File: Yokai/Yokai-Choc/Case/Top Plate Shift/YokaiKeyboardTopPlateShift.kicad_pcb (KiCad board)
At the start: 2 copper layers, 160.3 x 114.7 mm, 6 parts

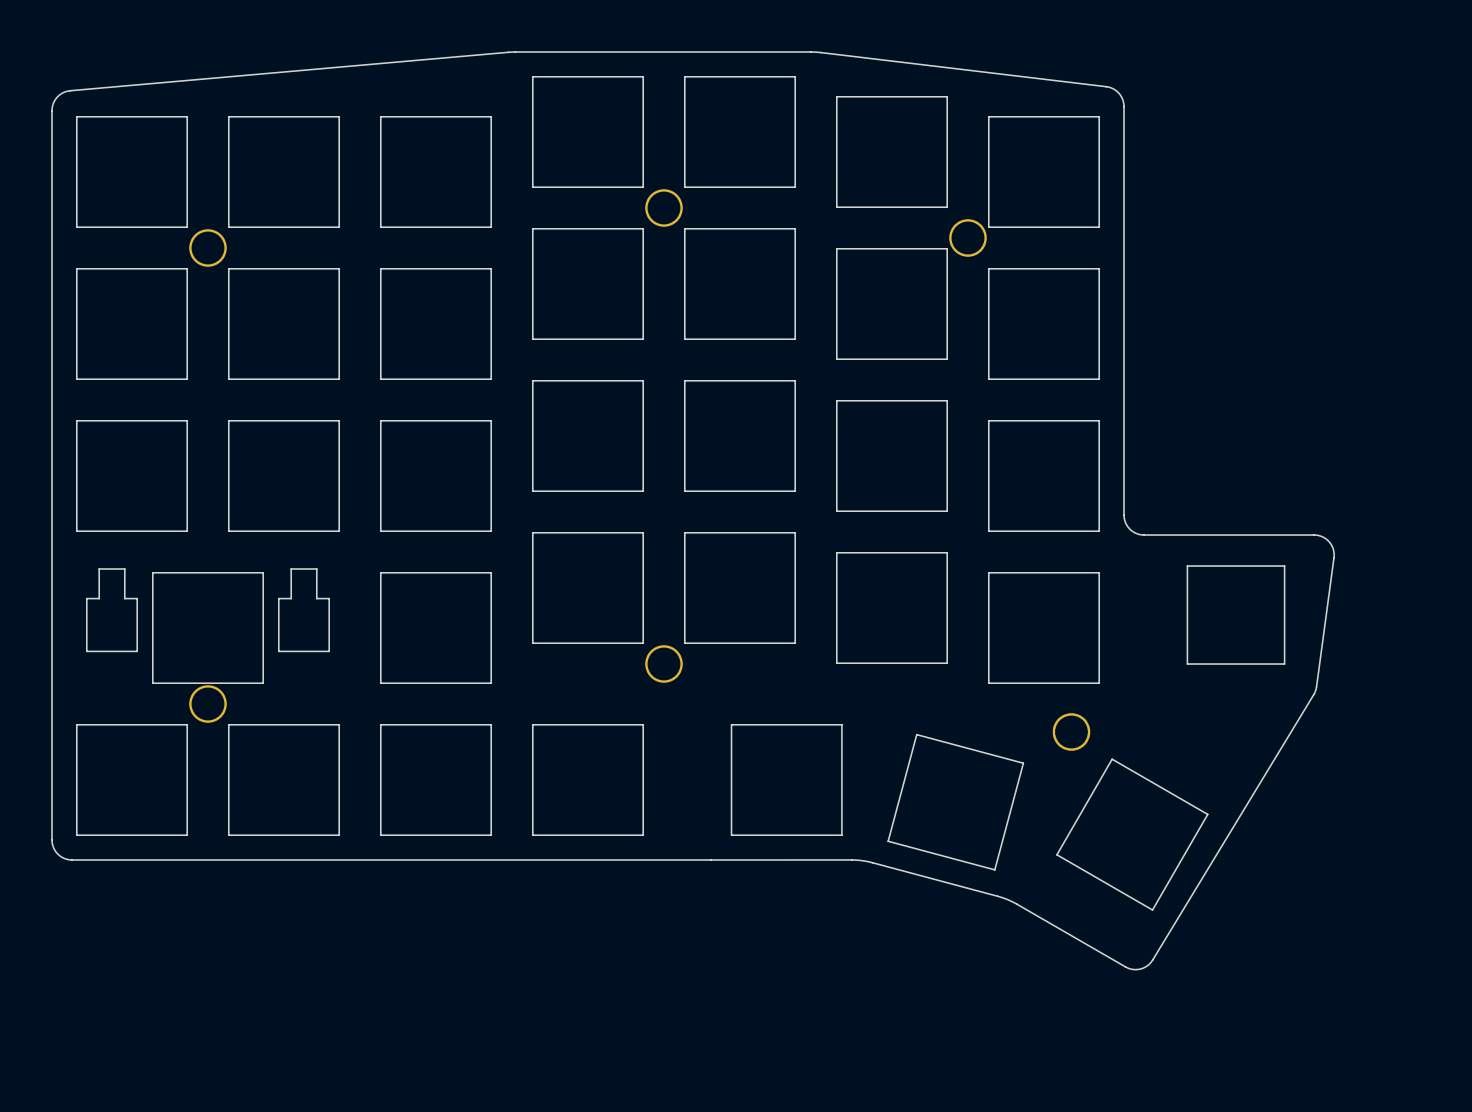
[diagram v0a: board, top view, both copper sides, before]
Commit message: Add files via upload
*Increased pinky stagger
*Inverted stabilizer cutouts
*Added additional thumb key
*Minor footprint changes
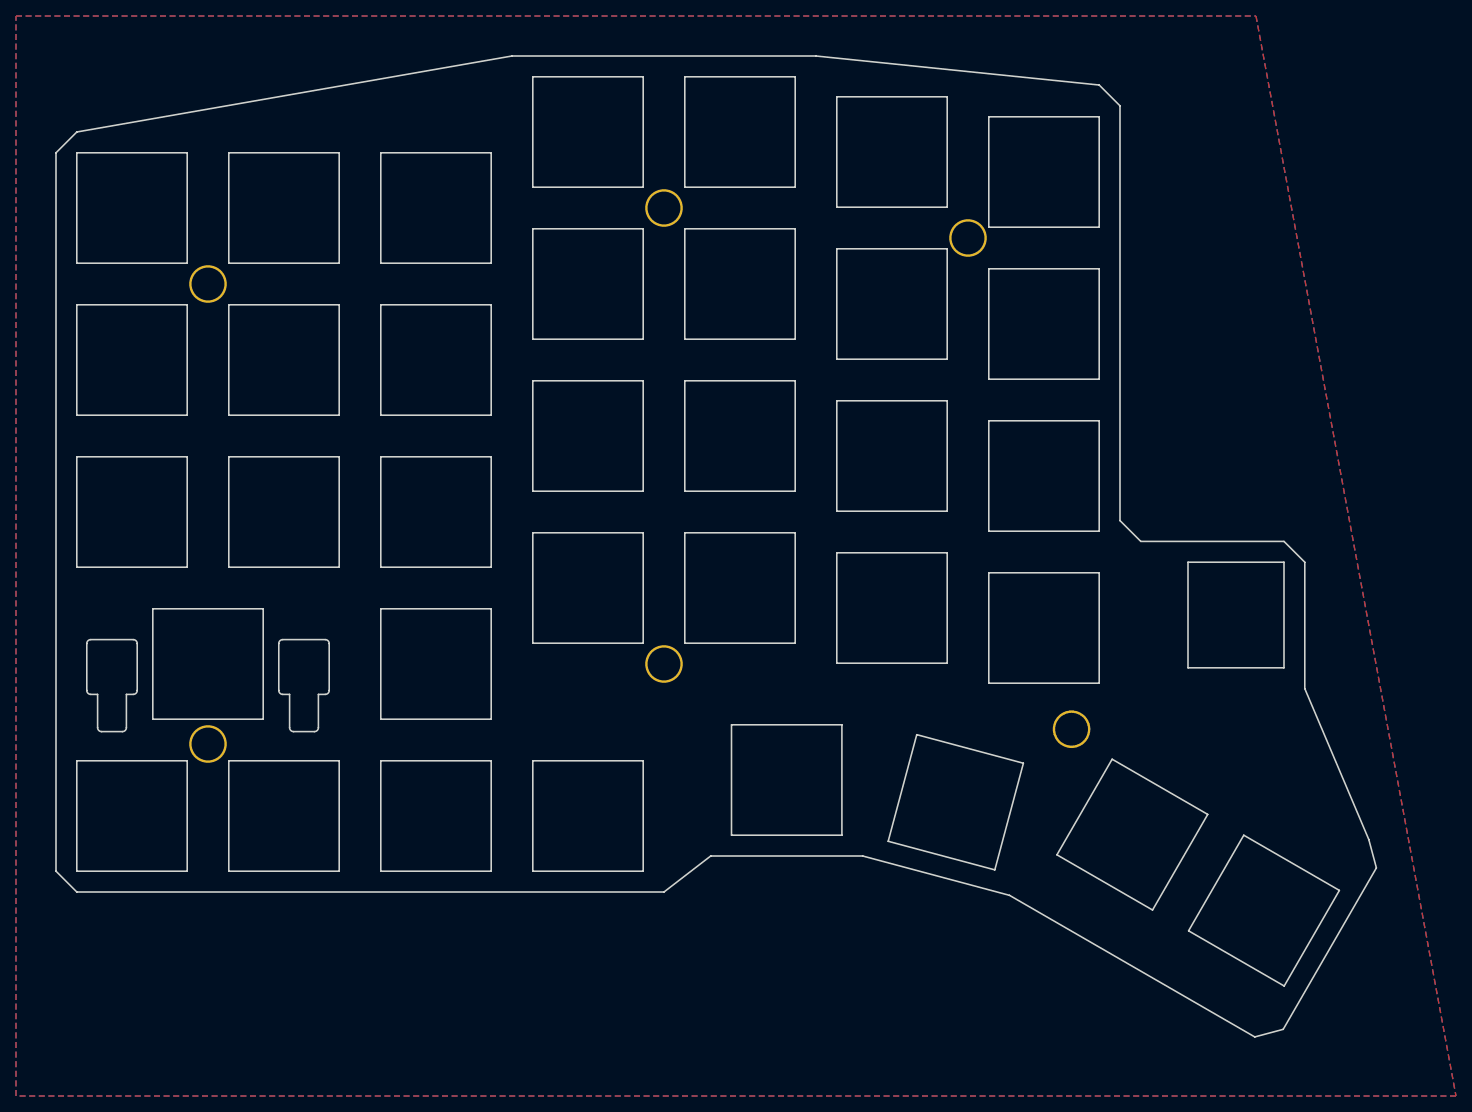
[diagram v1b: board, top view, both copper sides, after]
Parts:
- removed the TH5 at (79.0, 59.0)
- removed the TH5 at (79.0, 116.0)
- added TH5: HOLE, kbd:HOLE_M2_TH, F.Cu at (79.0, 63.5)
- added TH5: HOLE, kbd:HOLE_M2_TH, F.Cu at (79.0, 121.0)
- moved TH5 0.35 mm to (186.9, 119.2)
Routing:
- added copper zone on B.Cu, net (none)
- added copper zone on F.Cu, net (none)
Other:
- board size 160.3 x 114.7 mm -> 165.1 x 122.6 mm
